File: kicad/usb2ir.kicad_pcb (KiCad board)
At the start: 2 copper layers, 61 x 36.1 mm, 41 parts, among them J1 USB_A, J2 Conn_01x04_Male, Q1 S8050, Q2 S8050, SW1 SW_Push, U1 YK003, U2 CH340G, U3 LM1117-3.3, U4 STM32F103RBTx, Y1 12M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

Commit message: 硬件添加红外复制功能
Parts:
- added D4: 1N4148, Diode_SMD:D_0603_1608Metric_Castellated, F.Cu at (126.2, 93.2)
- added D5: 1N4148, Diode_SMD:D_0603_1608Metric_Castellated, F.Cu at (122.5, 96.7)
- added D6: IR204A, LED_THT:LED_D3.0mm_IRBlack, F.Cu at (115.4, 96.7)
- added Q3: S8050, Package_TO_SOT_SMD:SOT-23, F.Cu at (132.8, 98.0)
- added Q4: S8550, Package_TO_SOT_SMD:SOT-23, F.Cu at (126.3, 97.8)
- added R10: 10K, Resistor_SMD:R_0603_1608Metric_Pad1.05x0.95mm_HandSolder, F.Cu at (137.9, 98.0)
- added R11: 15K, Resistor_SMD:R_0603_1608Metric_Pad1.05x0.95mm_HandSolder, F.Cu at (129.9, 98.0)
- added R12: 12K, Resistor_SMD:R_0603_1608Metric_Pad1.05x0.95mm_HandSolder, F.Cu at (135.9, 97.9)
- added R13: 27K, Resistor_SMD:R_0603_1608Metric_Pad1.05x0.95mm_HandSolder, F.Cu at (126.2, 95.0)
- added R14: 1K, Resistor_SMD:R_0603_1608Metric_Pad1.05x0.95mm_HandSolder, F.Cu at (118.8, 96.7)
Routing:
- net +3V3: track 223.0 -> 269.2 mm, vias 8 -> 11
- net Net-(Q3-Pad1): track 0.00 -> 32.1 mm, vias 0 -> 3
- net Net-(Q3-Pad3): track 0.00 -> 29.2 mm, vias 0 -> 1
- net Net-(D4-Pad1): track 0.00 -> 13.2 mm, vias 0 -> 2
- net Net-(Q3-Pad2): track 0.00 -> 5.59 mm
- net Net-(D5-Pad2): track 0.00 -> 3.87 mm
- net Net-(D6-Pad1): track 0.00 -> 2.45 mm
- net Net-(D5-Pad1): track 0.00 -> 2.05 mm

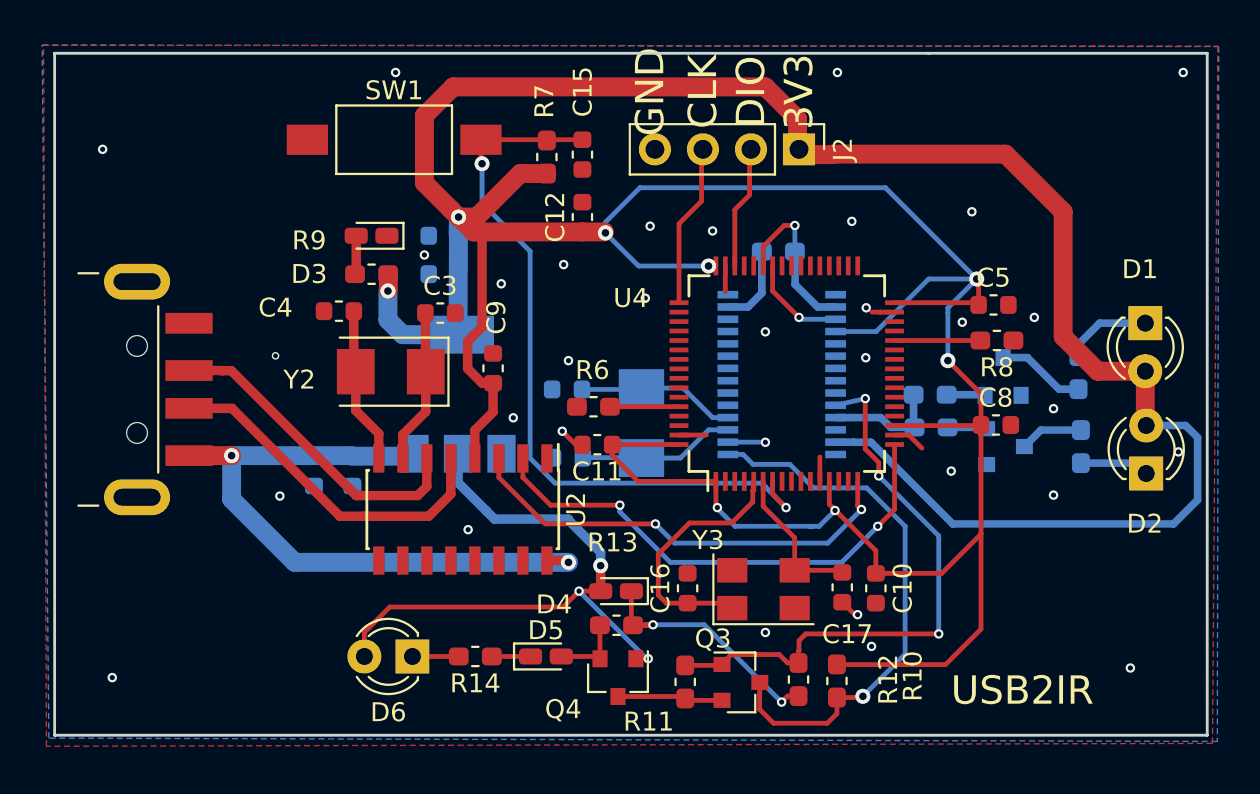
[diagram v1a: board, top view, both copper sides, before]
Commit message: 经过长时间的运行发现CH340G偶尔会出现数据丢失情况故现改用cp2104增加稳定性
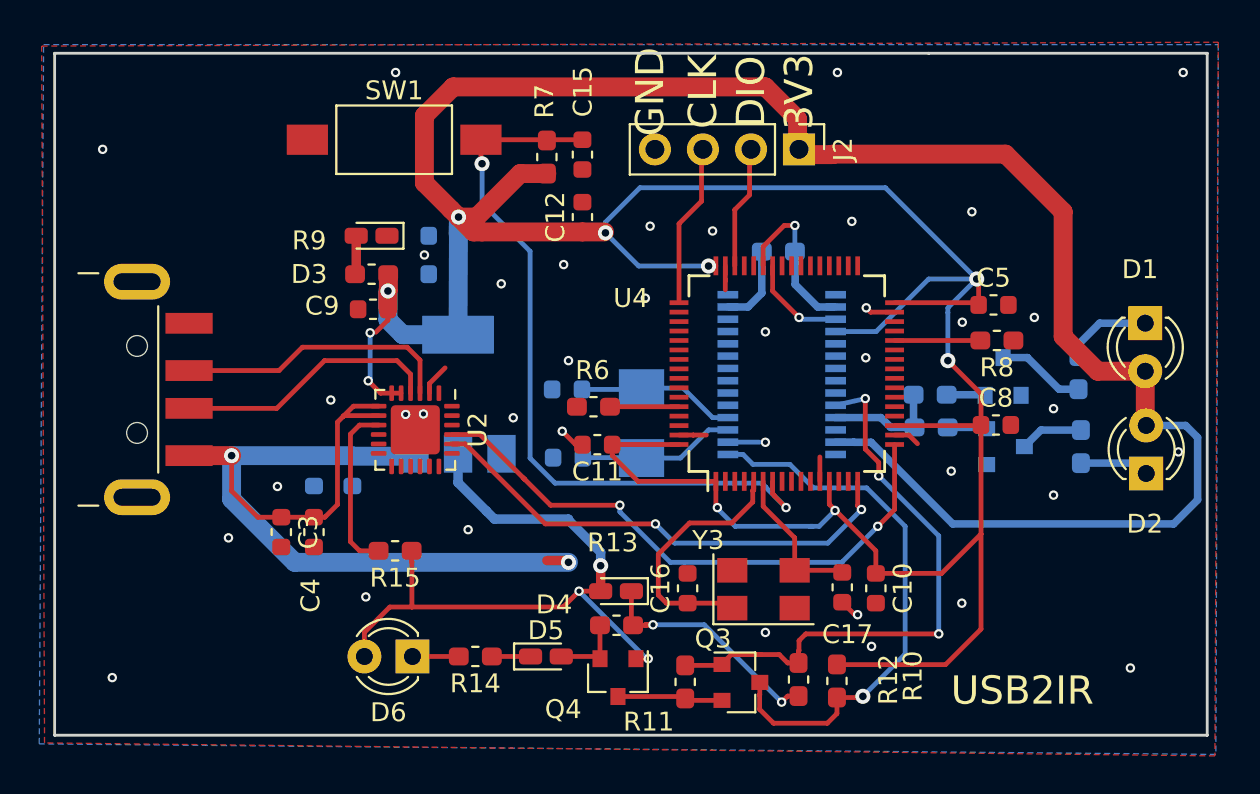
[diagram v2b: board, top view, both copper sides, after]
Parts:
- removed Y2: 12M, Crystal:Crystal_SMD_5032-2Pin_5.0x3.2mm
- added R15: 10K, Resistor_SMD:R_0603_1608Metric_Pad1.05x0.95mm_HandSolder, F.Cu at (114.5, 91.1)
- C3: value 22pF -> 10uf
- C4: value 22pF -> 104
- U2: value CH340G -> CP2104; footprint Package_SO:SOIC-16_3.9x9.9mm_P1.27mm -> Package_DFN_QFN:QFN-24-1EP_4x4mm_P0.5mm_EP2.6x2.6mm
- moved C3 14.3 mm to (108.5, 90.1), turned to 270 degrees
- moved C4 11.8 mm to (110.2, 90.1), turned to 270 degrees
- moved C9 7.08 mm to (113.4, 78.3), turned to 180 degrees
- moved U2 4.91 mm to (115.6, 84.7)
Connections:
- C3 pad 1: Net-(C3-Pad1) -> +5V
- C4 pad 1: Net-(C4-Pad1) -> +5V
- U2 pad 1: GND -> Net-(U2-Pad1)
- U2 pad 16: +5V -> Net-(U2-Pad16)
- U2 pad 2: /RXD2 -> GND
- U2 pad 3: /TXD2 -> /D+
- U2 pad 4: +3V3 -> /D-
- U2 pad 5: /D- -> +3V3
- U2 pad 6: /D+ -> +3V3
- U2 pad 7: Net-(C3-Pad1) -> +5V
- U2 pad 8: Net-(C4-Pad1) -> +5V
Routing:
- net +5V: track 34.6 -> 51.7 mm
- net Net-(R15-Pad2): track 0.00 -> 9.07 mm
- net Net-(C4-Pad1): track 8.34 -> 0.00 mm
- net Net-(C3-Pad1): track 8.20 -> 0.00 mm
- net /D-: track 18.6 -> 14.1 mm
- net /RXD2: track 27.3 -> 31.2 mm
- net +3V3: track 269.2 -> 265.6 mm, vias 11 -> 13
- net /D+: track 17.0 -> 14.8 mm
- net /TXD2: track 23.9 -> 26.1 mm
- net GND: track 11.1 -> 12.8 mm, vias 33 -> 38
